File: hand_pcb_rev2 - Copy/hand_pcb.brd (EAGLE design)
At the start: 65.2 x 60.5 mm, 70 parts

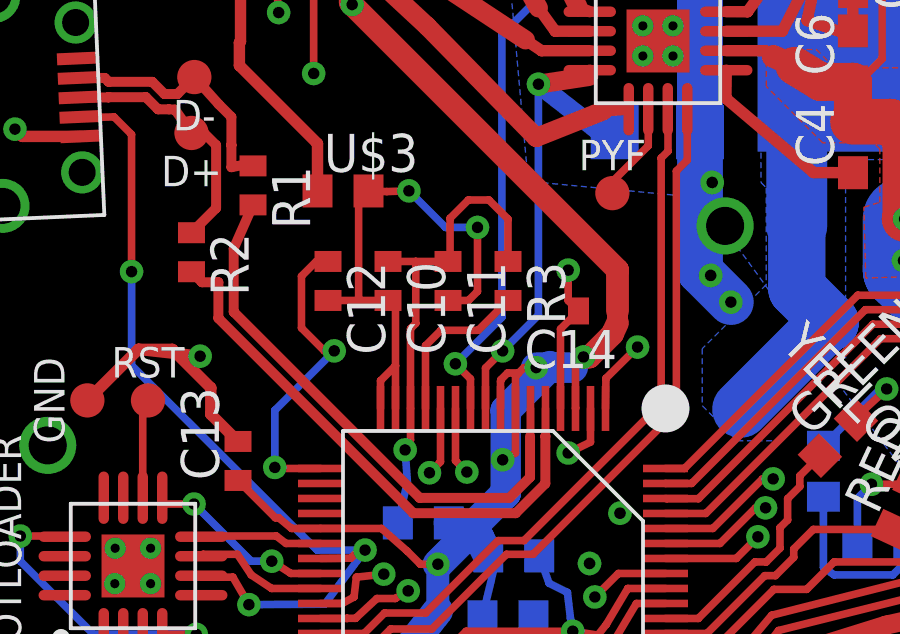
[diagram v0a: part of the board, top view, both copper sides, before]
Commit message: corrected some resistors and caps for the M04
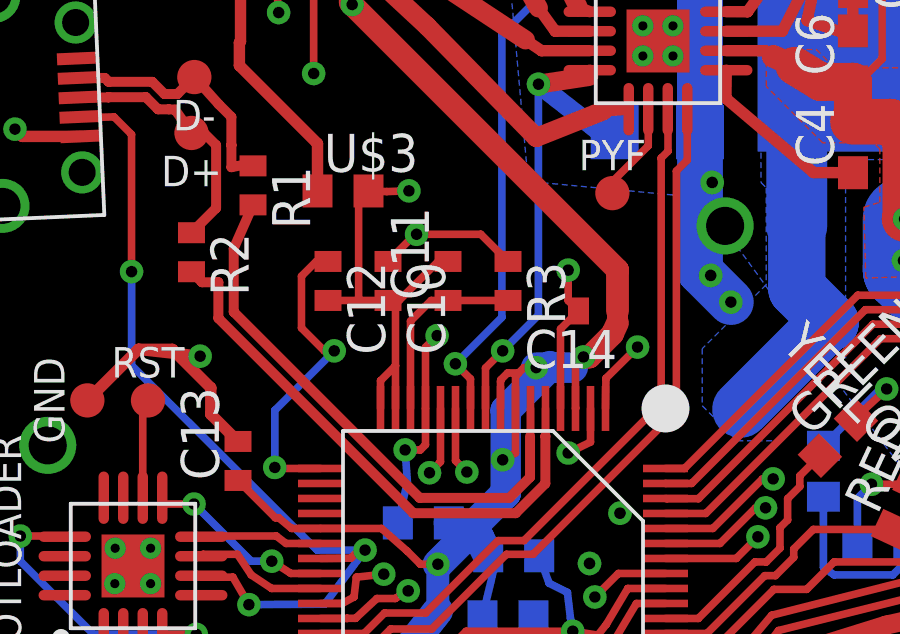
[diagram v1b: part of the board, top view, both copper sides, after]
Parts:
- turned C11 to 90 degrees
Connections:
- removed net N$32: HAND_MICRO.13, R3.2
- removed net N$33: C10.1, C11.1, HAND_MICRO.14, R3.1, U$4.2
- new net N$7: C10.1, HAND_MICRO.13, R3.1, U$4.2
- new net N$9: C11.1, HAND_MICRO.14, R3.2
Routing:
- net N$33: track 16.2 -> 0.00 mm, vias 1 -> 0
- net N$7: track 0.00 -> 15.4 mm, vias 0 -> 3
- net N$9: track 0.00 -> 6.45 mm
- net N$32: track 5.47 -> 0.00 mm
- net N$18: track 18.5 -> 15.0 mm, vias 2 -> 1
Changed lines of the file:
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@@
 <element name="R3" library="rcl" package="R0402" value="470" x="19" y="29" locked="yes" rot="R270"/>
 <element name="C10" library="rcl" package="C0402" value="2.2" x="15" y="29" locked="yes" rot="R270"/>
-<element name="C11" library="rcl" package="C0402" value="0.1" x="17" y="29" locked="yes" rot="R270"/>
+<element name="C11" library="rcl" package="C0402" value="0.1" x="17" y="29" rot="R90"/>
 <element name="C12" library="rcl" package="C0402" value="0.1" x="13" y="29" locked="yes" rot="R270"/>
 <element name="C13" library="rcl" package="C0402" value="0.1" x="10" y="23" locked="yes" rot="R90"/>
@@
 <wire x1="14.35" y1="32" x2="14.0208" y2="31.6708" width="0.254" layer="1"/>
 <wire x1="14.0208" y1="31.6708" x2="14.0208" y2="28.35" width="0.254" layer="1"/>
-<wire x1="17" y1="28.35" x2="17.682" y2="28.35" width="0.254" layer="1"/>
-<wire x1="17.682" y1="28.35" x2="17.9832" y2="28.6512" width="0.254" layer="1"/>
-<wire x1="17.9832" y1="28.6512" x2="17.9832" y2="30.7848" width="0.254" layer="1"/>
-<via x="17.9832" y="30.7848" extent="1-16" drill="0.381"/>
 <via x="15.6972" y="32.004" extent="1-16" drill="0.381"/>
 <wire x1="15.6972" y1="32.004" x2="14.9596" y2="31.9796" width="0.254" layer="1"/>
 <wire x1="14.9596" y1="31.9796" x2="14.35" y2="32" width="0.254" layer="1"/>
-<wire x1="15.6972" y1="32.004" x2="16.9164" y2="30.7848" width="0.254" layer="16"/>
-<wire x1="16.9164" y1="30.7848" x2="17.9832" y2="30.7848" width="0.254" layer="16"/>
 <wire x1="14.75" y1="24.75" x2="14.75" y2="25.6747" width="0.254" layer="1"/>
 <wire x1="14.75" y1="25.6747" x2="15.25" y2="26.1747" width="0.254" layer="1"/>
+<wire x1="17" y1="29.65" x2="16.6706" y2="29.65" width="0.254" layer="1"/>
+<wire x1="16.6706" y1="29.65" x2="15.3706" y2="28.35" width="0.254" layer="1"/>
+<wire x1="15.3706" y1="28.35" x2="15" y2="28.35" width="0.254" layer="1"/>
 </signal>
 <signal name="USB_D2_N" class="1">
@@
 <wire x1="17.6022" y1="17.3228" x2="21.1582" y2="17.3228" width="0.254" layer="1"/>
 </signal>
-<signal name="N$32">
-<contactref element="HAND_MICRO" pad="13"/>
-<contactref element="R3" pad="2"/>
-<wire x1="19" y1="28.35" x2="18.0058" y2="27.3558" width="0.254" layer="1"/>
-<wire x1="18.0058" y1="27.3558" x2="16.764" y2="27.3558" width="0.254" layer="1"/>
-<wire x1="16.764" y1="27.3558" x2="16.25" y2="26.8418" width="0.254" layer="1"/>
-<wire x1="16.25" y1="26.8418" x2="16.25" y2="24.75" width="0.254" layer="1"/>
-</signal>
-<signal name="N$33">
-<contactref element="R3" pad="1"/>
-<contactref element="C10" pad="1"/>
-<contactref element="C11" pad="1"/>
-<contactref element="HAND_MICRO" pad="14"/>
-<contactref element="U$4" pad="2"/>
-<wire x1="17" y1="29.65" x2="15.9258" y2="29.65" width="0.254" layer="1"/>
-<wire x1="15.9258" y1="29.65" x2="15" y2="29.65" width="0.254" layer="1"/>
-<wire x1="15.75" y1="24.75" x2="15.75" y2="27.4086" width="0.254" layer="1"/>
-<wire x1="15.75" y1="27.4086" x2="15.9258" y2="27.5844" width="0.254" layer="1"/>
-<wire x1="15.9258" y1="27.5844" x2="15.9258" y2="29.65" width="0.254" layer="1"/>
-<wire x1="17" y1="29.65" x2="17.0688" y2="29.7188" width="0.254" layer="1"/>
-<wire x1="17.0688" y1="29.7188" x2="17.0688" y2="31.0896" width="0.254" layer="1"/>
-<wire x1="17.0688" y1="31.0896" x2="17.6784" y2="31.6992" width="0.254" layer="1"/>
-<wire x1="17.6784" y1="31.6992" x2="18.3642" y2="31.6992" width="0.254" layer="1"/>
-<wire x1="18.3642" y1="31.6992" x2="19" y2="31.0634" width="0.254" layer="1"/>
-<wire x1="19" y1="31.0634" x2="19" y2="29.65" width="0.254" layer="1"/>
-<wire x1="15.75" y1="24.75" x2="15.75" y2="23.6962" width="0.254" layer="1"/>
-<wire x1="15.75" y1="23.6962" x2="15.5702" y2="23.368" width="0.254" layer="1"/>
-<via x="15.5702" y="23.368" extent="1-16" drill="0.381"/>
-<wire x1="15.5702" y1="23.368" x2="15.6464" y2="22.2972" width="0.254" layer="16"/>
-<wire x1="15.6464" y1="22.2972" x2="15.3276" y2="20.937" width="0.254" layer="16"/>
-</signal>
 <signal name="N$34">
 <contactref element="HAND_MICRO" pad="17"/>
@@
 <wire x1="24.9728" y1="10.825" x2="24.0792" y2="9.9314" width="0.254" layer="1"/>
 </signal>
+<signal name="N$7">
+<contactref element="R3" pad="1"/>
+<contactref element="C10" pad="1"/>
+<contactref element="U$4" pad="2"/>
+<contactref element="HAND_MICRO" pad="13"/>
+<via x="15.5702" y="23.368" extent="1-16" drill="0.381"/>
+<wire x1="15.5702" y1="23.368" x2="15.6464" y2="22.2972" width="0.254" layer="16"/>
+<wire x1="15.6464" y1="22.2972" x2="15.3276" y2="20.937" width="0.254" layer="16"/>
+<wire x1="16.25" y1="24.75" x2="16.25" y2="23.5398" width="0.254" layer="1"/>
+<wire x1="16.25" y1="23.5398" x2="16.0782" y2="23.368" width="0.254" layer="1"/>
+<wire x1="16.0782" y1="23.368" x2="15.5702" y2="23.368" width="0.254" layer="1"/>
+<wire x1="19" y1="29.65" x2="18.0938" y2="30.5562" width="0.254" layer="1"/>
+<wire x1="18.0938" y1="30.5562" x2="15.9512" y2="30.5562" width="0.254" layer="1"/>
+<wire x1="15.9512" y1="30.5562" x2="15.9062" y2="30.5562" width="0.254" layer="1"/>
+<wire x1="15.9062" y1="30.5562" x2="15" y2="29.65" width="0.254" layer="1"/>
+<wire x1="16.25" y1="24.75" x2="16.25" y2="26.791" width="0.254" layer="1"/>
+<wire x1="16.25" y1="26.791" x2="16.637" y2="27.178" width="0.254" layer="1"/>
+<via x="16.637" y="27.178" extent="1-16" drill="0.381"/>
+<wire x1="16.637" y1="27.178" x2="16.637" y2="29.8704" width="0.254" layer="2"/>
+<wire x1="16.637" y1="29.8704" x2="15.9512" y2="30.5562" width="0.254" layer="2"/>
+<via x="15.9512" y="30.5562" extent="1-16" drill="0.381"/>
+</signal>
+<signal name="N$9">
+<contactref element="HAND_MICRO" pad="14"/>
+<contactref element="R3" pad="2"/>
+<contactref element="C11" pad="1"/>
+<wire x1="19" y1="28.35" x2="17" y2="28.35" width="0.254" layer="1"/>
+<wire x1="15.75" y1="24.75" x2="15.75" y2="27.6626" width="0.254" layer="1"/>
+<wire x1="15.75" y1="27.6626" x2="16.4374" y2="28.35" width="0.254" layer="1"/>
+<wire x1="16.4374" y1="28.35" x2="17" y2="28.35" width="0.254" layer="1"/>
+</signal>
 </signals>

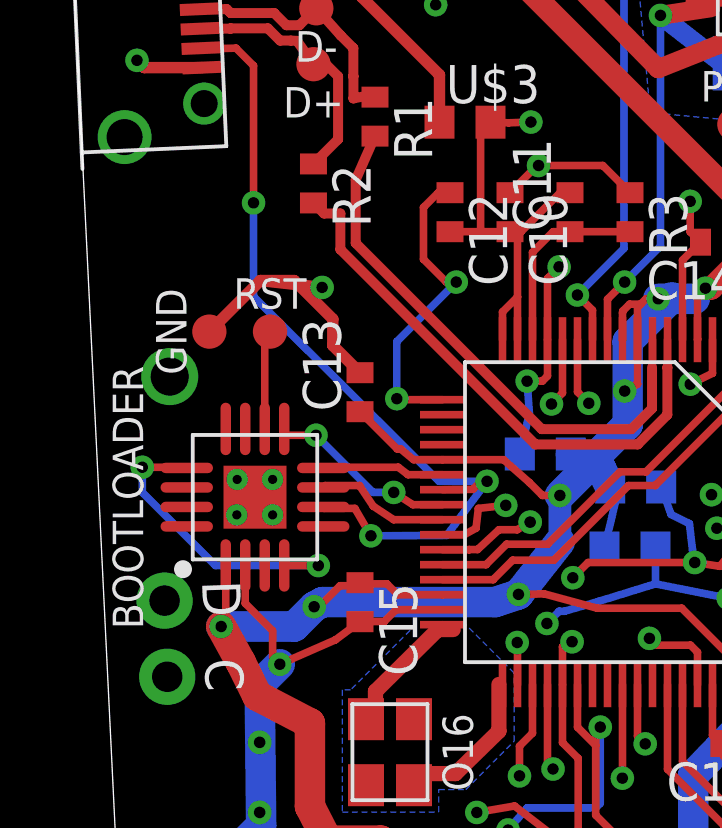
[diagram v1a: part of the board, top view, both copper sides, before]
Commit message: fixed bootloader
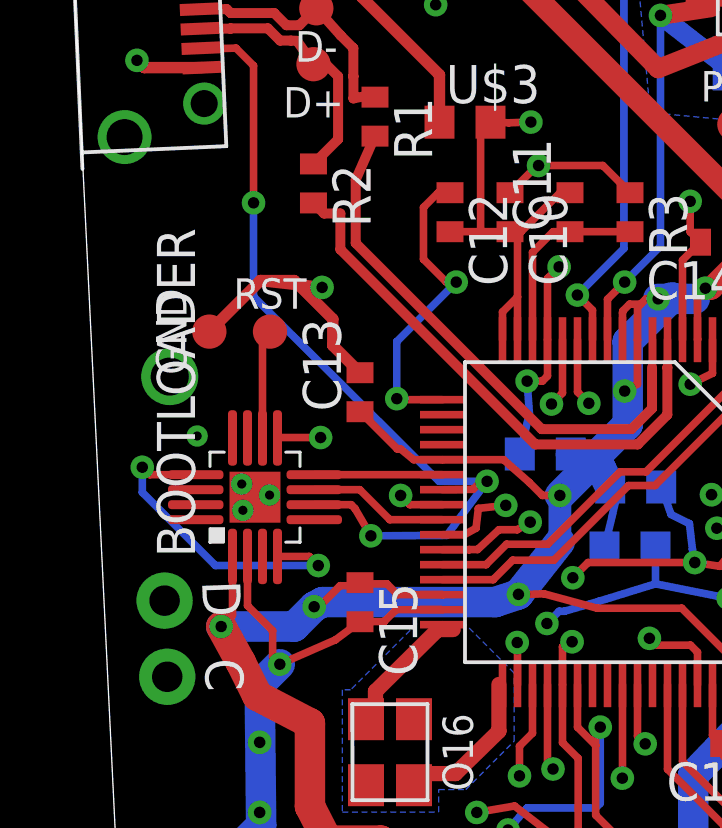
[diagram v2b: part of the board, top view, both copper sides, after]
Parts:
- BOOTLOADER: value MKL02Z32 -> MKL02Z32CORRECT; device 445-eagle-lib:WQFN-16 -> 445-eagle-lib:QFN16
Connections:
- net GND: now also BOOTLOADER.TH; no longer BOOTLOADER.PPAD
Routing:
- net N$17: track 19.4 -> 20.2 mm

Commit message: updated capacitor values for bypass caps to 10u, cleaned up schematic, updated tanalum cap value for linear regulator
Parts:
- C11, C12, C13, C14, C15, C16, C19: value 0.1 -> 10u
- C17: value (none) -> 10u
- C18: value (none) -> 50u
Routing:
- net GND: track 416.9 -> 406.8 mm, vias 46 -> 45
